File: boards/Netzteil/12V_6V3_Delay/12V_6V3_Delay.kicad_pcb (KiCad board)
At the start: 2 copper layers, 160 x 100 mm, 112 parts, among them J1 OP_LED, P1 12V5_AC, P10 6V3_DC_1, P11 Relais, P12 Relais, P13 Relais, P2 12V_DC_1, P3 12V_DC_2, P4 7V5_AC, P5 12V_DC_3, P6 12V_DC_4, P8 12V_DC_4, P9 6V3_DC_2, Q1 IRF530, Q2 IRF530, Q3 BS170, Q4 BS170, Q5 BS170, U1 LMC6484, U2 LM7812CT, U3 LM393, U4 LM393

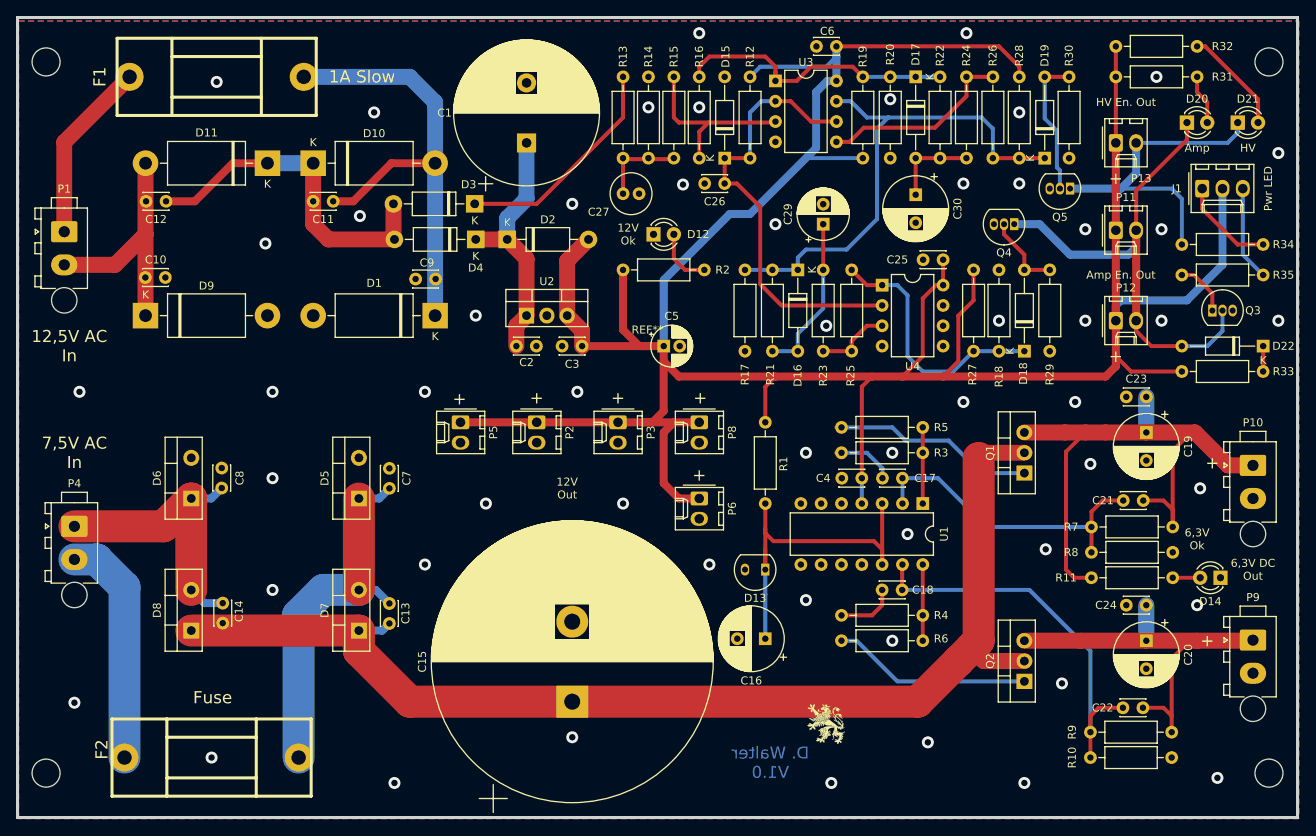
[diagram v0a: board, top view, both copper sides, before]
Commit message: Reworked Delay + Layout changed
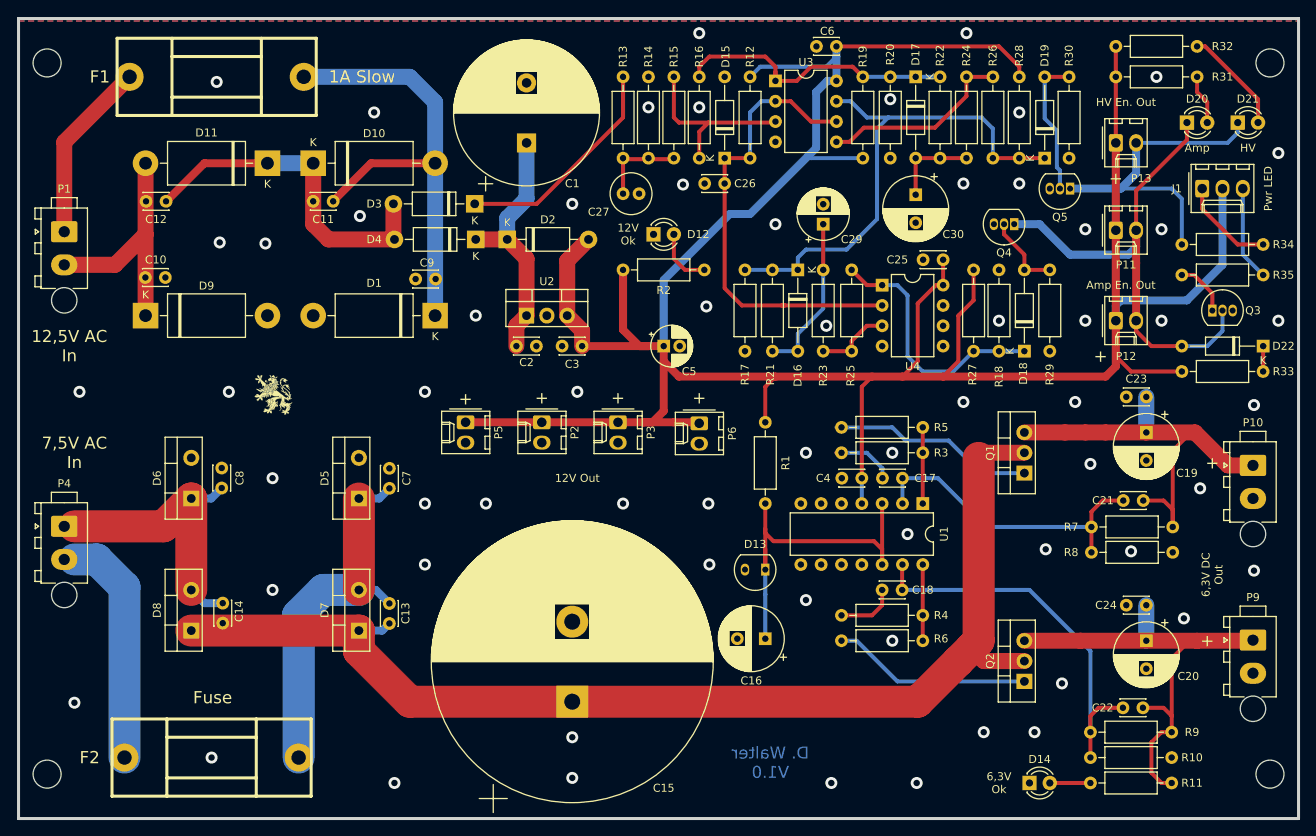
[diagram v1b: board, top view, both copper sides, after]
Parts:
- removed P8: 12V_DC_4, Connector_Molex:Molex_KK-254_AE-6410-02A_1x02_P2.54mm_Vertical
- moved G*** 80.4 mm to (86.5, 84.8)
- moved D14 35.0 mm to (181.0, 133.3), turned to 0 degrees
- moved R11 27.5 mm to (198.8, 133.3), turned to 180 degrees
- moved P6 9.40 mm to (139.7, 88.4)
- moved P4 1.27 mm to (60.3, 101.3)
- moved P2 0.64 mm to (120.0, 88.3)
- moved P5 0.63 mm to (110.5, 88.3)
- moved REF** 0.18 mm to (54.6, 137.8)
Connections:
- R11 pad 1: Net-(C19-Pad1) -> Net-(C20-Pad1)
- U1 pad 10: (no net) -> GND
- U1 pad 5: (no net) -> GND
- U1 pad 6: (no net) -> GND
- U1 pad 9: (no net) -> GND
- U4 pad 5: (no net) -> GND
- U4 pad 6: (no net) -> GND
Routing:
- net Net-(C19-Pad1): track 76.7 -> 55.0 mm
- net +12V: track 372.4 -> 358.4 mm
- net Net-(C20-Pad1): track 50.4 -> 60.3 mm
- net /Delay/Vref: track 56.1 -> 58.5 mm
- net Net-(D14-Pad2): track 3.43 -> 5.08 mm
- net GND: vias 55 -> 63

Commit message: Work in progess - many LAyour changes
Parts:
- removed the C16 at (148.0, 115.3)
- removed the C24 at (193.1, 111.1)
- removed D22: ZD5V6, Diode_THT:D_DO-35_SOD27_P10.16mm_Horizontal
- removed the P11 at (191.8, 64.3)
- removed the Q3 at (203.8, 74.3)
- added C14: 680µF/16V, Capacitor_THT:CP_Radial_D8.0mm_P3.50mm, F.Cu at (148.0, 109.9)
- added C23: 100nF, Capacitor_THT:C_Disc_D3.0mm_W2.0mm_P2.50mm, F.Cu at (200.0, 113.0)
- added J2: Standby, Connector_Molex:Molex_KK-254_AE-6410-02A_1x02_P2.54mm_Vertical, F.Cu at (132.7, 90.8)
- added J3: Standby, Connector_Molex:Molex_KK-254_AE-6410-02A_1x02_P2.54mm_Vertical, F.Cu at (141.0, 90.8)
- added J4: Conn_01x03, Connector_Molex:Molex_KK-254_AE-6410-03A_1x03_P2.54mm_Vertical, F.Cu at (200.7, 76.2)
- added J5: Standby, Connector_Molex:Molex_KK-254_AE-6410-02A_1x02_P2.54mm_Vertical, F.Cu at (137.2, 99.7)
- added P9: Relais, Connector_Molex:Molex_KK-254_AE-6410-02A_1x02_P2.54mm_Vertical, F.Cu at (191.8, 65.4)
- added Q5: BC557, Package_TO_SOT_THT:TO-92_Inline, F.Cu at (200.7, 59.7)
- added Q6: BC557, Package_TO_SOT_THT:TO-92_Inline, F.Cu at (200.7, 65.4)
- C27: footprint Capacitor_THT:C_Radial_D5.0mm_H11.0mm_P2.00mm -> Capacitor_THT:CP_Radial_D5.0mm_P2.00mm
- J1: value OP_LED -> Chassis_GND; footprint Connector_Molex:Molex_KK-254_AE-6410-03A_1x03_P2.54mm_Vertical -> MountingHole:MountingHole_3.2mm_M3_Pad_Via
- R34: value 560R -> 10K
- R35: value 680R -> 100R
- moved J1 134.6 mm to (70.5, 85.1)
- moved R35 57.6 mm to (143.3, 79.4), turned to 90 degrees
- moved P5 20.0 mm to (120.0, 85.1)
- moved R33 17.6 mm to (211.5, 68.6), turned to 90 degrees
- moved G*** 17.4 mm to (86.4, 102.2)
- moved R1 14.0 mm to (139.8, 79.4), turned to 90 degrees
- moved P2 10.8 mm to (110.5, 93.3)
- moved P3 10.8 mm to (120.0, 93.3)
- moved R34 8.03 mm to (207.6, 68.6), turned to 90 degrees
- moved C22 7.20 mm to (200.0, 87.0), turned to 270 degrees
- moved Q3 7.10 mm to (186.1, 64.8)
- moved D20 6.48 mm to (207.0, 52.1)
- moved D21 6.48 mm to (200.7, 52.1)
- moved D8 3.30 mm to (137.3, 64.8)
- moved D13 3.18 mm to (148.0, 103.5)
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- renumbered C9 to C1, C7 to C10, C8 to C11, C13 to C12, C14 to C13, C17 to C16, C18 to C17, C19 to C18, C20 to C19, C10 to C2, C21 to C20, C22 to C21, C23 to C22, C6 to C24, C26 to C25, C25 to C26, C29 to C28, C30 to C29, C11 to C3, C12 to C4, C1 to C5, C2 to C6, C3 to C7, C5 to C8, C4 to C9, D6 to D10, D7 to D11, D8 to D12, D9 to D2, D10 to D3, D11 to D4, D3 to D5, D4 to D6, D2 to D7, D12 to D8, D5 to D9, P12 to P10, P13 to P11, P5 to P4, P6 to P5, P4 to P6, P9 to P7, P10 to P8, Q4 to Q3, Q5 to Q4, R2 to R1, R19 to R17, R20 to R18, R21 to R19, R1 to R2, R22 to R20, R23 to R21, R24 to R22, R25 to R23, R26 to R24, R27 to R25, R18 to R26, R28 to R27, R17 to R28, U2 to U1, U1 to U2
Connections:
- J1 pad 1: /Delay/LED_G -> GND
- R33 pad 1: +12V -> Net-(Q5-Pad2)
- R33 pad 2: Net-(D22-Pad1) -> Net-(D20-Pad1)
- R34 pad 1: Net-(D21-Pad1) -> Net-(Q6-Pad2)
- R34 pad 2: /Delay/LED_G -> Net-(D21-Pad1)
- R35 pad 2: /Delay/LED_R -> Net-(D16-Pad1)
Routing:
- net Net-(J2-Pad1): track 6.92 -> 34.4 mm
- net Net-(Q5-Pad2): track 0.00 -> 16.6 mm
- net /6V3/Reference: track 45.7 -> 36.3 mm
- net Net-(D21-Pad1): track 41.2 -> 32.3 mm
- net Net-(D20-Pad1): track 62.9 -> 54.4 mm
- net Net-(Q6-Pad2): track 0.00 -> 8.15 mm
- net Net-(C18-Pad1): track 55.0 -> 48.5 mm
- net Net-(D20-Pad2): track 6.24 -> 12.0 mm
- net /Delay/LED_R: track 11.8 -> 17.6 mm
- net Net-(C19-Pad1): track 60.3 -> 55.9 mm
- net Net-(D16-Pad1): track 64.4 -> 68.7 mm
- net Net-(D22-Pad1): track 3.18 -> 0.00 mm
- net Net-(D8-Pad2): track 7.44 -> 4.45 mm
- net Net-(D18-Pad2): track 9.94 -> 7.62 mm
- net /Delay/Vref: track 58.5 -> 56.4 mm
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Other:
- board text added: "Chassis GND"
- board text added: "G"
- board text added: "R"
- board text added: "Standby"

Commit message: Update
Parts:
- removed R28: 10K, Resistor_THT:R_Axial_DIN0207_L6.3mm_D2.5mm_P10.16mm_Horizontal
- removed R35: 100R, Resistor_THT:R_Axial_DIN0207_L6.3mm_D2.5mm_P10.16mm_Horizontal
- added D22: LED, LED_THT:LED_D3.0mm, F.Cu at (181.0, 107.7)
- C28: value 56µF / 16V -> 220µF / 16V; footprint Capacitor_THT:CP_Radial_D6.3mm_P2.50mm -> Capacitor_THT:CP_Radial_D8.0mm_P3.50mm
- Q5: value BC557 -> BC337
- R19: value 470K -> 330K
- R20: value 620K -> 220K
- R26: value 10K -> 270R
- R29, R30: value 10K -> 100K
- R33, R34: value 10K -> 4k7
- U2: value LMC6484 -> LMC6482; footprint Package_DIP:DIP-14_W7.62mm -> Package_DIP:DIP-8_W7.62mm
- moved G*** 82.6 mm to (163.8, 130.8)
- moved R26 35.0 mm to (198.9, 107.7), turned to 180 degrees
- moved C9 13.9 mm to (170.1, 101.4), turned to -90 degrees
- moved R33 10.2 mm to (211.5, 58.4), turned to -90 degrees
- moved D8 8.29 mm to (136.5, 73.0)
- moved C17 4.43 mm to (158.1, 109.2)
- moved D13 3.81 mm to (151.8, 103.5)
- moved R2 3.81 mm to (151.8, 98.4)
- moved D18 3.18 mm to (178.4, 79.4)
- moved R29 3.17 mm to (181.6, 69.2)
- moved R1 3.05 mm to (142.9, 79.4)
- moved C14 2.54 mm to (150.5, 109.9)
- moved Q6 2.54 mm to (203.2, 65.4), turned to 180 degrees
- moved C16 1.92 mm to (160.7, 95.2)
- moved U2 1.91 mm to (165.7, 98.4)
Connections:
- D17 pad 1: Net-(D17-Pad1) -> Net-(D16-Pad1)
- D19 pad 1: Net-(D16-Pad1) -> Net-(D19-Pad1)
- J2 pad 1: Net-(J2-Pad1) -> Net-(C28-Pad1)
- J3 pad 1: Net-(J2-Pad1) -> Net-(C28-Pad1)
- J5 pad 1: Net-(J2-Pad1) -> Net-(C28-Pad1)
- Q5 pad 2: Net-(Q5-Pad2) -> Net-(D20-Pad1)
- Q6 pad 1: +12V -> /Delay/LED_G
- Q6 pad 3: /Delay/LED_G -> +12V
- R16 pad 1: Net-(D17-Pad1) -> Net-(D16-Pad1)
- R17 pad 1: Net-(D17-Pad1) -> Net-(D16-Pad1)
- R18 pad 2: Net-(D17-Pad1) -> Net-(D16-Pad1)
- R20 pad 1: Net-(D17-Pad1) -> Net-(D16-Pad1)
- R24 pad 2: Net-(D16-Pad1) -> Net-(D19-Pad1)
- R26 pad 1: Net-(D18-Pad1) -> Net-(C18-Pad1)
- R26 pad 2: GND -> Net-(D22-Pad2)
- R27 pad 2: Net-(D16-Pad1) -> Net-(D19-Pad1)
- R33 pad 1: Net-(Q5-Pad2) -> Net-(D20-Pad1)
- R33 pad 2: Net-(D20-Pad1) -> +12V
- U2 pad 4: +12V -> GND
- U2 pad 5: GND -> /6V3/Reference
- U2 pad 6: GND -> Net-(C17-Pad2)
- U2 pad 7: (no net) -> Net-(R4-Pad2)
- U2 pad 8: (no net) -> +12V
- U3 pad 1: Net-(D17-Pad1) -> Net-(D16-Pad1)
- U3 pad 7: Net-(D16-Pad1) -> Net-(D19-Pad1)
- U4 pad 7: (no net) -> unconnected-(U4-Pad7)
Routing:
- net Net-(C28-Pad1): track 19.1 -> 60.1 mm
- net Net-(D17-Pad1): track 36.6 -> 0.00 mm
- net +12V: track 356.6 -> 391.2 mm
- net Net-(J2-Pad1): track 34.4 -> 0.00 mm
- net Net-(D19-Pad1): track 0.00 -> 31.1 mm
- net Net-(Q5-Pad2): track 16.6 -> 0.00 mm
- net Net-(C18-Pad1): track 48.5 -> 56.6 mm
- net /6V3/Reference: track 36.3 -> 29.8 mm
- net Net-(D22-Pad2): track 0.00 -> 5.22 mm
- net Net-(C17-Pad1): track 7.51 -> 3.45 mm
- net Net-(D16-Pad1): track 68.7 -> 64.7 mm, vias 0 -> 1
- net Net-(R4-Pad2): track 9.52 -> 12.9 mm
- net Net-(D18-Pad1): track 33.4 -> 30.2 mm
- net Net-(C17-Pad2): track 49.7 -> 52.5 mm
- net Net-(D20-Pad1): track 54.4 -> 57.1 mm
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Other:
- net class Default removed
- board text added: "-"

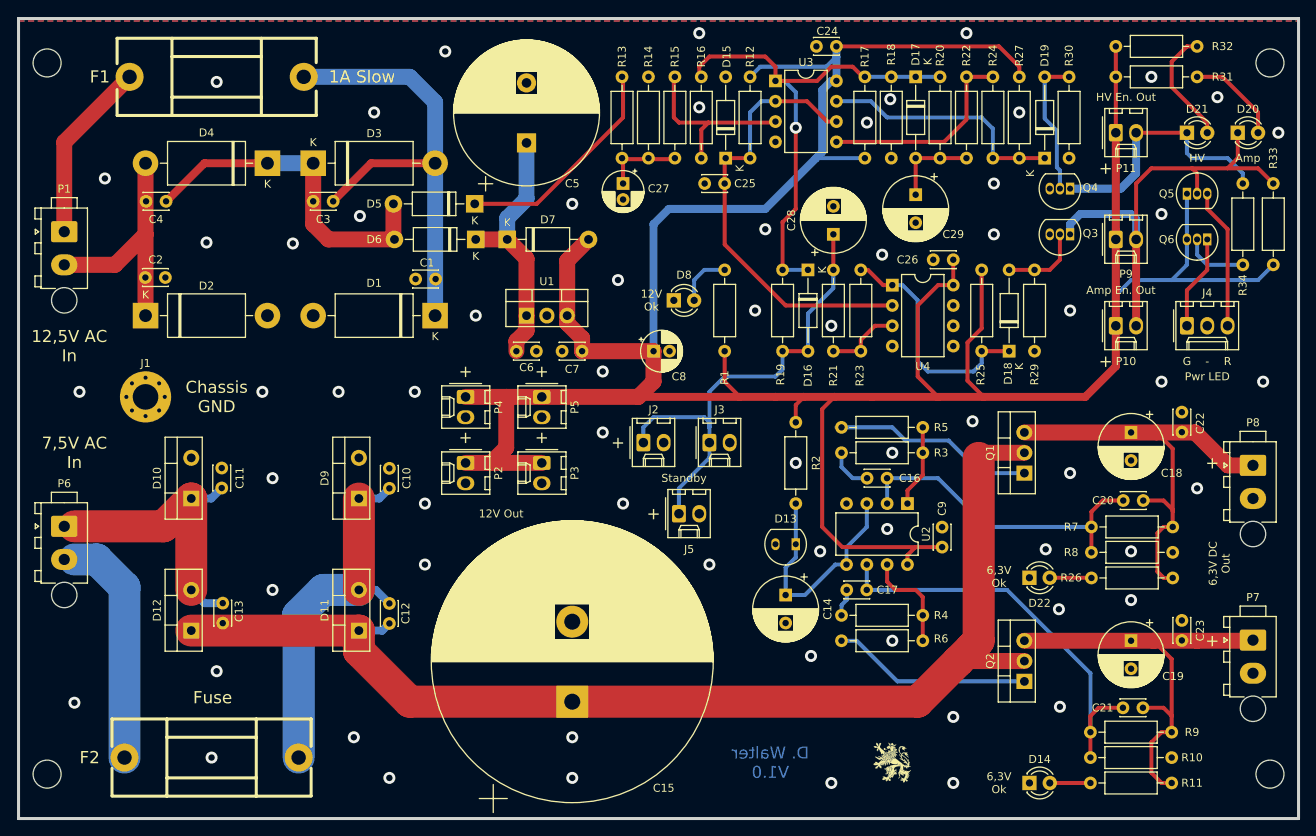
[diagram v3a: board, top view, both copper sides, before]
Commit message: 6.3V, 400V und 400V Regler Boards bestellt
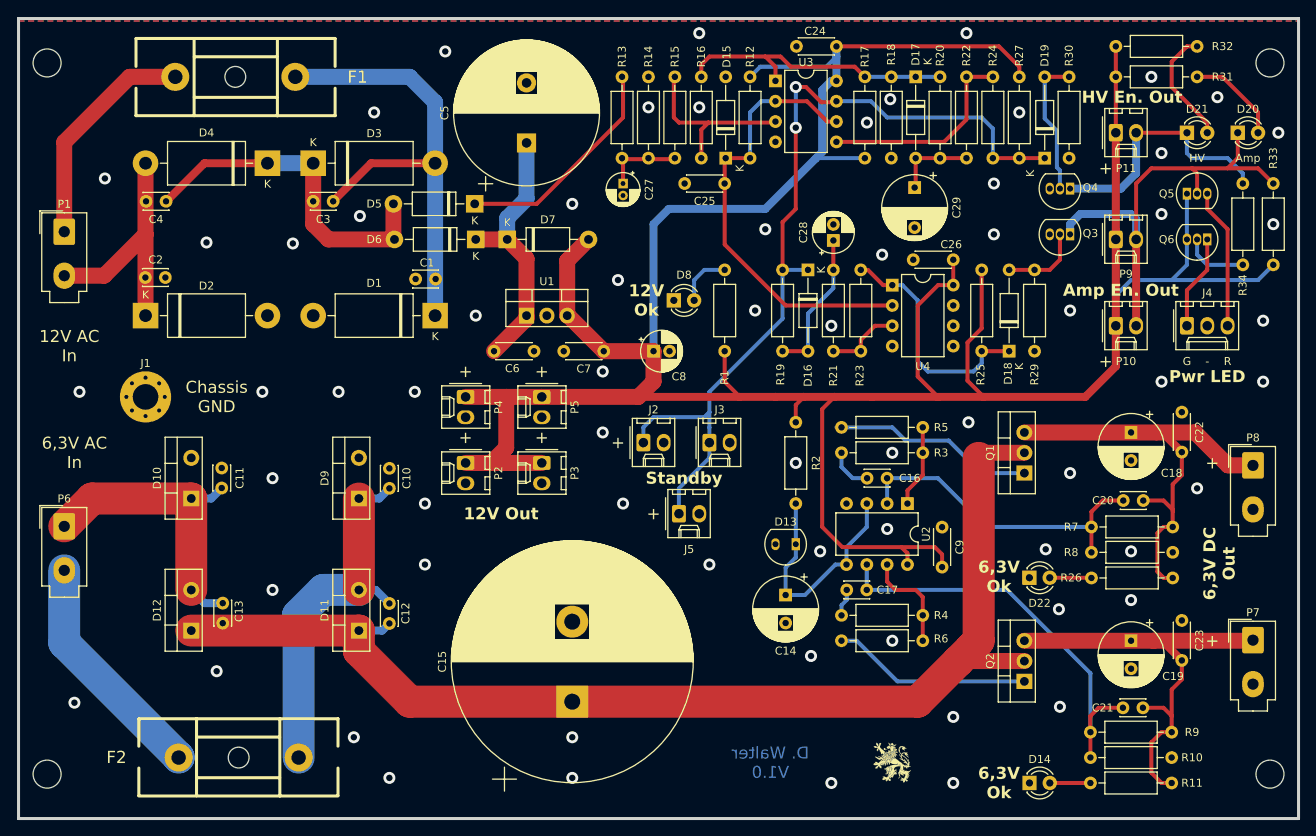
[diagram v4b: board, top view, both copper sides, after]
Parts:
- C15: footprint Capacitor_THT:CP_Radial_D35.0mm_P10.00mm_SnapIn -> Capacitor_THT:CP_Radial_D30.0mm_P10.00mm_SnapIn
- C22, C23, C24, C25, C26, C6, C9: footprint Capacitor_THT:C_Disc_D3.0mm_W2.0mm_P2.50mm -> Capacitor_THT:C_Disc_D4.3mm_W1.9mm_P5.00mm
- C27: footprint Capacitor_THT:CP_Radial_D5.0mm_P2.00mm -> Capacitor_THT:CP_Radial_D4.0mm_P1.50mm
- C28: value 220µF / 16V -> 10µF / 16V; footprint Capacitor_THT:CP_Radial_D8.0mm_P3.50mm -> Capacitor_THT:CP_Radial_D5.0mm_P2.00mm
- C29: value 220µF / 16V -> 330µF / 16V; footprint Capacitor_THT:CP_Radial_D8.0mm_P3.50mm -> Capacitor_THT:CP_Radial_D8.0mm_P5.00mm
- C7: value 100nF / 16V -> Fuse; footprint Capacitor_THT:C_Disc_D3.0mm_W2.0mm_P2.50mm -> Capacitor_THT:C_Disc_D4.3mm_W1.9mm_P5.00mm
- F1: value 1A Slow -> Fuse; footprint w_misc_comp:fuse_holder_CQ-2 -> Fuse_Holder_Eska:Fuse_Holder_Eska_509200
- F2: footprint w_misc_comp:fuse_holder_CQ-2 -> Fuse_Holder_Eska:Fuse_Holder_Eska_509200
- P1, P6, P7, P8: footprint Connector_TE-Connectivity:TE_MATE-N-LOK_1-770866-x_1x02_P4.14mm_Vertical -> Connector_Molex:Molex_Mini-Fit_Jr_5566-02A_2x01_P4.20mm_Vertical
- moved F1 5.72 mm to (85.1, 45.1)
- moved C6 2.79 mm to (114.0, 79.4)
- moved C7 2.71 mm to (127.8, 79.4)
- moved C29 0.90 mm to (166.6, 58.9)
- moved C28 0.76 mm to (156.5, 65.5)
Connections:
- C28 pad 1: Net-(C28-Pad1) -> Net-(D16-A)
- D16 pad 1: Net-(D16-Pad1) -> Net-(D16-K)
- D16 pad 2: Net-(C28-Pad1) -> Net-(D16-A)
- D17 pad 1: Net-(D16-Pad1) -> Net-(D17-K)
- D19 pad 1: Net-(D19-Pad1) -> Net-(D16-K)
- J2 pad 1: Net-(C28-Pad1) -> Net-(D16-K)
- J3 pad 1: Net-(C28-Pad1) -> Net-(D16-K)
- J5 pad 1: Net-(C28-Pad1) -> Net-(D16-K)
- R16 pad 1: Net-(D16-Pad1) -> Net-(D17-K)
- R17 pad 1: Net-(D16-Pad1) -> Net-(D17-K)
- R18 pad 2: Net-(D16-Pad1) -> Net-(D17-K)
- R19 pad 1: Net-(D16-Pad1) -> Net-(D16-K)
- R19 pad 2: Net-(C28-Pad1) -> Net-(D16-A)
- R20 pad 1: Net-(D16-Pad1) -> Net-(D17-K)
- R21 pad 1: Net-(C28-Pad1) -> Net-(D16-A)
- R24 pad 2: Net-(D19-Pad1) -> Net-(D16-K)
- R27 pad 2: Net-(D19-Pad1) -> Net-(D16-K)
- U3 pad 1: Net-(D16-Pad1) -> Net-(D17-K)
- U3 pad 7: Net-(D19-Pad1) -> Net-(D16-K)
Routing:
- net Net-(D16-K): track 0.00 -> 110.6 mm, vias 0 -> 2
- net Net-(D16-Pad1): track 64.7 -> 0.00 mm, vias 1 -> 0
- net Net-(C28-Pad1): track 60.1 -> 0.00 mm
- net Net-(D17-K): track 0.00 -> 36.5 mm
- net Net-(D19-Pad1): track 31.1 -> 0.00 mm
- net Net-(D16-A): track 0.00 -> 18.3 mm
- net Net-(P1-P1): track 22.7 -> 28.5 mm
- net Net-(P7-P1): track 55.8 -> 57.5 mm
- net Net-(D10-K): track 36.4 -> 37.7 mm
- net Net-(D6-K): track 32.5 -> 33.7 mm
- net Net-(P8-P1): track 56.6 -> 57.7 mm
- net Net-(D1-K): track 59.1 -> 60.2 mm
- net Net-(D17-A): track 10.9 -> 10.1 mm
- net Net-(D2-K): track 30.8 -> 31.4 mm
- net GND: vias 64 -> 67
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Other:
- board text added: "12V AC In"
- board text added: "6,3V AC In"
- board text removed: "12,5V AC In"
- board text removed: "7,5V AC In"
